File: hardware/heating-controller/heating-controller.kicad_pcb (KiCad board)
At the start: 2 copper layers, 81.8 x 85.9 mm, 22 parts, among them J1 LilyGo T-Display S3, J2 Temperature_probes, J3 Power connector, K1 FINDER-32.21-x000, Q1 AO3400A, U1 H11AA1

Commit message: First PCB, needs to be checked
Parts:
- added R1: 15k, Resistor_SMD:R_0603_1608Metric, F.Cu at (31.2, 17.8)
- added R5: 15k, Resistor_SMD:R_0603_1608Metric, F.Cu at (31.2, 22.5)
- C1: renamed from C2; footprint Resistor_SMD:R_0201_0603Metric -> Capacitor_SMD:C_0603_1608Metric
- moved R6 8.68 mm to (53.7, 45.6), turned to 0 degrees
- moved R4 0.85 mm to (31.8, 58.0)
- moved C1 0.23 mm to (43.4, 29.8)
- renumbered C3 to C2, C1 to C3, F2 to F1, F1 to F2, R3 to R2, R2 to R3, R1 to R4, R4 to R6, R5 to R7, R6 to R8, RV2 to RV1, RV1 to RV2
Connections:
- J2 pad 1: /EXT_TEMP_1 -> /EXT_TEMP
- J2 pad 3: /LIM_TEMP_1 -> /LIMITER_TEMP
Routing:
- net /LIMITER_TEMP: track 0.00 -> 111.6 mm, vias 0 -> 4
- net /EXT_TEMP: track 0.00 -> 102.1 mm, vias 0 -> 4
- net /RELAY_CMD: track 84.2 -> 96.4 mm
- net +3.3V: track 69.0 -> 58.2 mm
- net /HP_ACTIVE: track 74.3 -> 66.7 mm, vias 0 -> 2
- net +5V: track 96.5 -> 94.3 mm
- net /REL_NO: track 20.2 -> 18.2 mm
- net /REL_COM: track 36.4 -> 35.2 mm

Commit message: WIP
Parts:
- added D1: 1N4148WS, Diode_SMD:D_SOD-323, F.Cu at (74.8, 41.0)
- added D3: LED, LED_SMD:LED_0805_2012Metric, F.Cu at (95.2, 62.0)
- added J4: EXT_LED, Connector_PinHeader_2.54mm:PinHeader_1x02_P2.54mm_Vertical, F.Cu at (90.0, 63.6)
- added R7: 470, Resistor_SMD:R_0603_1608Metric, F.Cu at (85.8, 61.0)
- added R9: 470, Resistor_SMD:R_0603_1608Metric, F.Cu at (93.4, 59.1)
- C3: renamed from C2; footprint Capacitor_THT:C_Radial_D6.3mm_H7.0mm_P2.50mm -> Capacitor_THT:C_Radial_D10.0mm_H12.5mm_P5.00mm
- J1: renamed from J2; footprint Connector_Phoenix_MSTB:PhoenixContact_MSTBVA_2,5_4-G_1x04_P5.00mm_Vertical -> TerminalBlock_Phoenix:TerminalBlock_Phoenix_MKDS-3-4-5.08_1x04_P5.08mm_Horizontal
- J3: footprint Connector_Phoenix_MSTB:PhoenixContact_MSTBVA_2,5_7-G_1x07_P5.00mm_Vertical -> TerminalBlock_Phoenix:TerminalBlock_Phoenix_MKDS-3-7-5.08_1x07_P5.08mm_Horizontal
- R5: renamed from R2; footprint Resistor_THT:R_Axial_DIN0204_L3.6mm_D1.6mm_P5.08mm_Horizontal -> Resistor_THT:R_Axial_DIN0614_L14.3mm_D5.7mm_P15.24mm_Horizontal
- moved R5 41.8 mm to (29.1, 65.1), turned to 90 degrees
- moved RV2 35.6 mm to (24.1, 70.8)
- moved Q1 32.9 mm to (83.2, 88.2), turned to -90 degrees
- moved R8 32.4 mm to (78.2, 65.9)
- moved J2 31.7 mm to (46.8, 35.7)
- moved F2 31.6 mm to (25.3, 84.6)
- moved C3 30.3 mm to (68.0, 59.2)
- moved C2 29.2 mm to (64.5, 50.0)
- moved J3 28.9 mm to (25.7, 100.5)
- moved D2 28.7 mm to (64.6, 54.3)
- moved C1 28.5 mm to (75.1, 78.7)
- moved RV1 28.5 mm to (44.4, 79.7)
- moved PS1 28.5 mm to (36.0, 47.4)
- moved R2 28.5 mm to (48.9, 74.6)
- moved R3 28.5 mm to (52.0, 78.1)
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- renumbered C3 to C1, C1 to C2, D1 to D2, D2 to D4, F2 to F1, F1 to F2, J1 to J2, R8 to R10, R3 to R2, R4 to R3, R5 to R4, R7 to R8, RV2 to RV1, RV1 to RV2
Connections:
- J2 pad 12: +5V -> Net-(D1-Pad1)
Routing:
- net +3.3V: track 58.2 -> 10.0 mm
- net /RELAY_CMD: track 96.4 -> 49.6 mm
- net Net-(D3-Pad1): track 7.67 -> 50.2 mm
- net /EXT_TEMP: track 102.1 -> 123.8 mm, vias 4 -> 0
- net Net-(Q1-Pad1): track 6.73 -> 28.0 mm, vias 0 -> 2
- net /HP_ACTIVE: track 66.7 -> 77.0 mm
- net Net-(F2-Pad2): track 27.8 -> 18.8 mm
- net /REL_COM: track 35.2 -> 27.7 mm
- net +5V: track 94.3 -> 101.4 mm, vias 0 -> 2
- net /L: track 22.7 -> 16.1 mm
- net /LIMITER_TEMP: track 111.6 -> 118.1 mm, vias 4 -> 0
- net /N: track 54.3 -> 48.7 mm
- net Net-(F1-Pad2): track 19.5 -> 14.4 mm
- net Net-(D1-Pad1): track 0.00 -> 4.21 mm
- net Net-(J4-Pad2): track 0.00 -> 3.42 mm
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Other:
- outline, holes or cut-outs redrawn
- board text added: "https://github.com/BwanaFr/heating-controller"

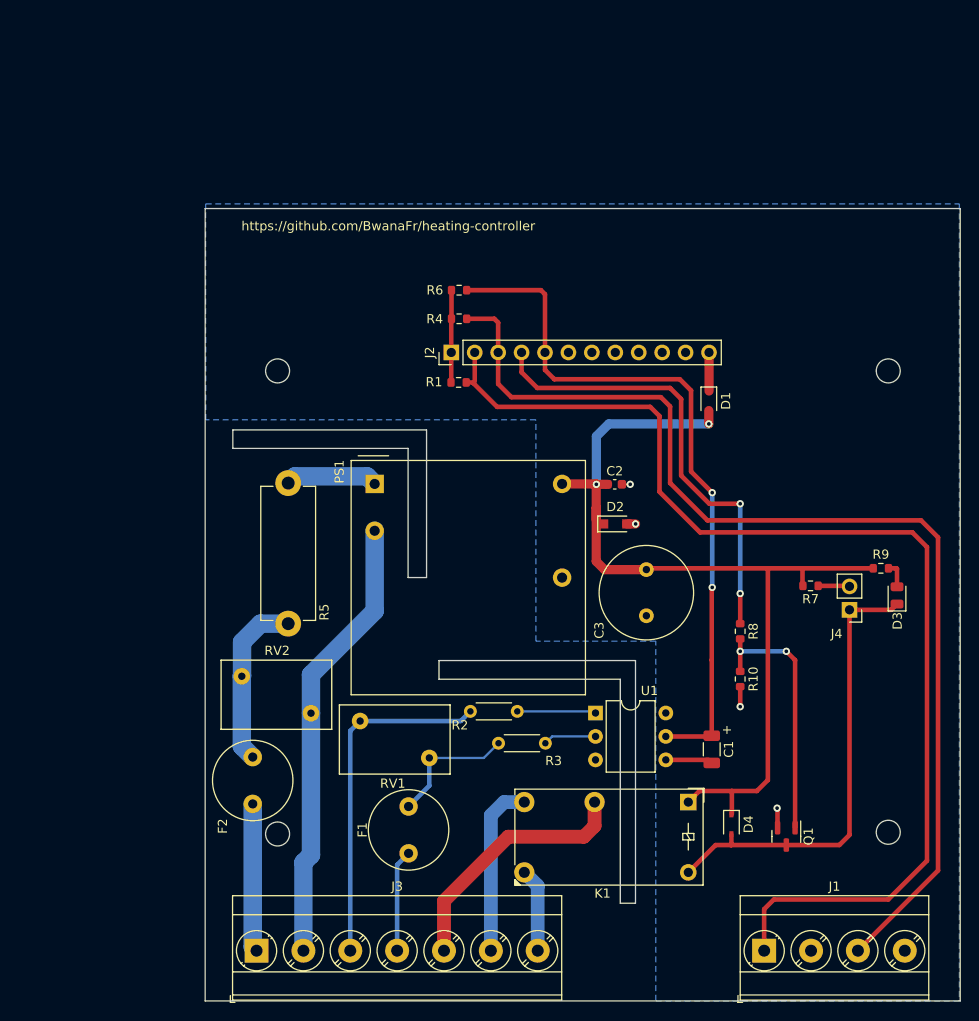
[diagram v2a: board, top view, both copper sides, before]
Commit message: Added 10uF capacitors to NTC
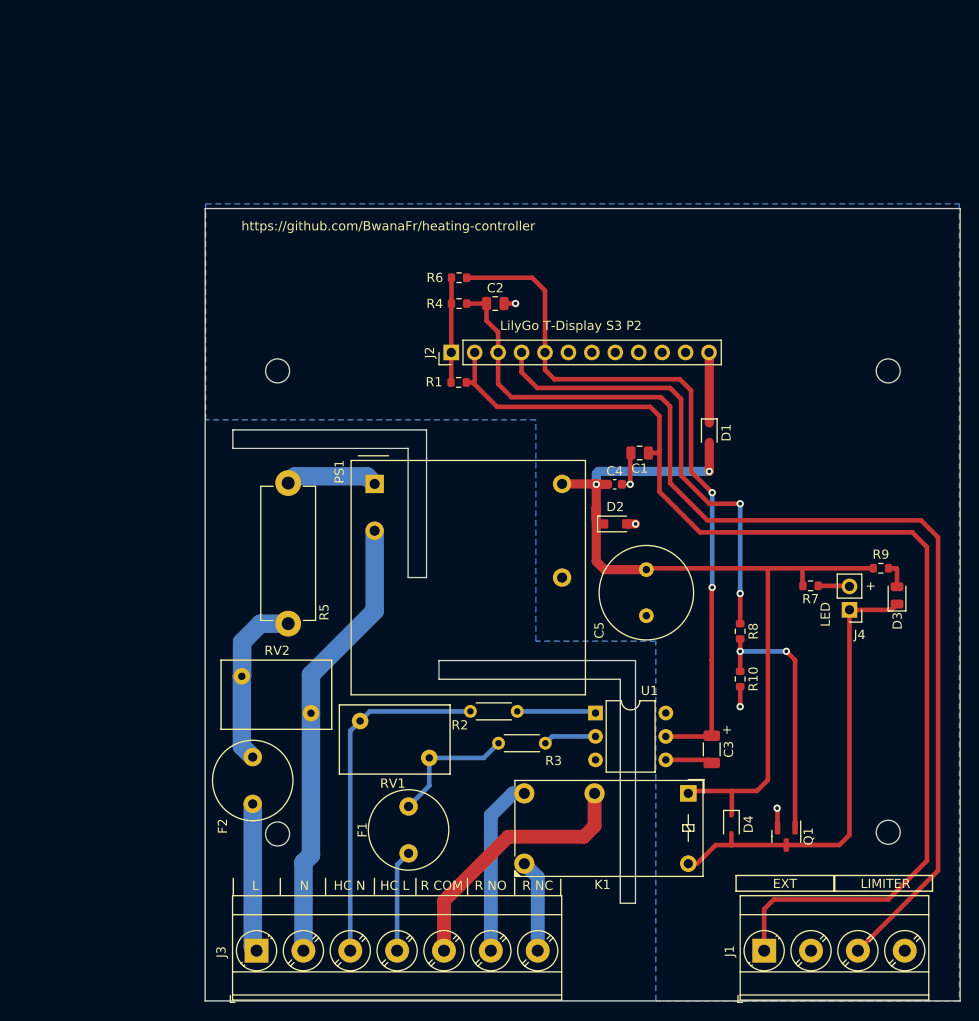
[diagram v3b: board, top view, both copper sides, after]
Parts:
- added C1: 10uF, Capacitor_SMD:C_0805_2012Metric, F.Cu at (67.2, 46.6)
- added C2: 10uF, Capacitor_SMD:C_0805_2012Metric, F.Cu at (51.6, 30.4)
- moved D1 3.45 mm to (74.8, 44.4)
- moved R4 1.65 mm to (47.7, 30.4)
- moved R6 1.35 mm to (47.7, 27.6)
- moved K1 0.94 mm to (72.5, 83.5)
- renumbered C1 to C3, C2 to C4, C3 to C5
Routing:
- net GND: track 11.3 -> 16.0 mm, vias 4 -> 5
- net Net-(D1-Pad1): track 4.21 -> 7.66 mm
- net +5V: track 101.4 -> 98.3 mm
- net +3.3V: track 10.0 -> 11.4 mm
- net /EXT_TEMP: track 123.8 -> 125.1 mm
- net /LIMITER_TEMP: track 118.1 -> 119.2 mm
- net /REL_NC: track 9.09 -> 10.0 mm
- net /REL_COM: track 27.7 -> 28.6 mm
- net /HP_ACTIVE: track 77.0 -> 77.8 mm
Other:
- board text added: "EXT"
- board text added: "HC L"
- board text added: "HC N"
- board text added: "L"
- board text added: "LED"
- board text added: "LIMITER"
- board text added: "LilyGo T-Display S3 P2"
- board text added: "N"
- board text added: "R COM"
- board text added: "R NC"
- board text added: "R NO"

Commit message: WIP
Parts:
- added J5: USER_LED, Connector_PinHeader_2.54mm:PinHeader_1x02_P2.54mm_Vertical, F.Cu at (87.8, 44.6)
- added Q1: AO3400A, Package_TO_SOT_SMD:SOT-23, F.Cu at (82.8, 44.6)
- added R11: 100k, Resistor_SMD:R_0603_1608Metric, F.Cu at (78.5, 44.7)
- added R13: 470, Resistor_SMD:R_0603_1608Metric, F.Cu at (82.1, 49.7)
- added R8: 1k, Resistor_SMD:R_0603_1608Metric, F.Cu at (81.8, 39.6)
- R10: renamed from R9; value 470 -> 2k
- renumbered D3 to D2, D2 to D3, Q1 to Q2, R10 to R12, R8 to R9
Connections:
- J1 pad 2: /EXT_TEMP_2 -> GND
- J1 pad 4: /LIM_TEMP_2 -> GND
- J2 pad 6: unconnected-(J2-Pad6) -> /USER_LED
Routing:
- net /USER_LED: track 0.00 -> 31.5 mm
- net Net-(J5-Pad2): track 0.00 -> 7.23 mm
- net +5V: track 98.3 -> 105.3 mm
- net Net-(Q1-Pad1): track 0.00 -> 6.71 mm
- net Net-(J5-Pad1): track 0.00 -> 4.12 mm
- net GND: track 16.0 -> 19.4 mm, vias 5 -> 6
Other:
- board text added: "REL_LED"
- board text added: "USER_LED"
- board text removed: "LED"

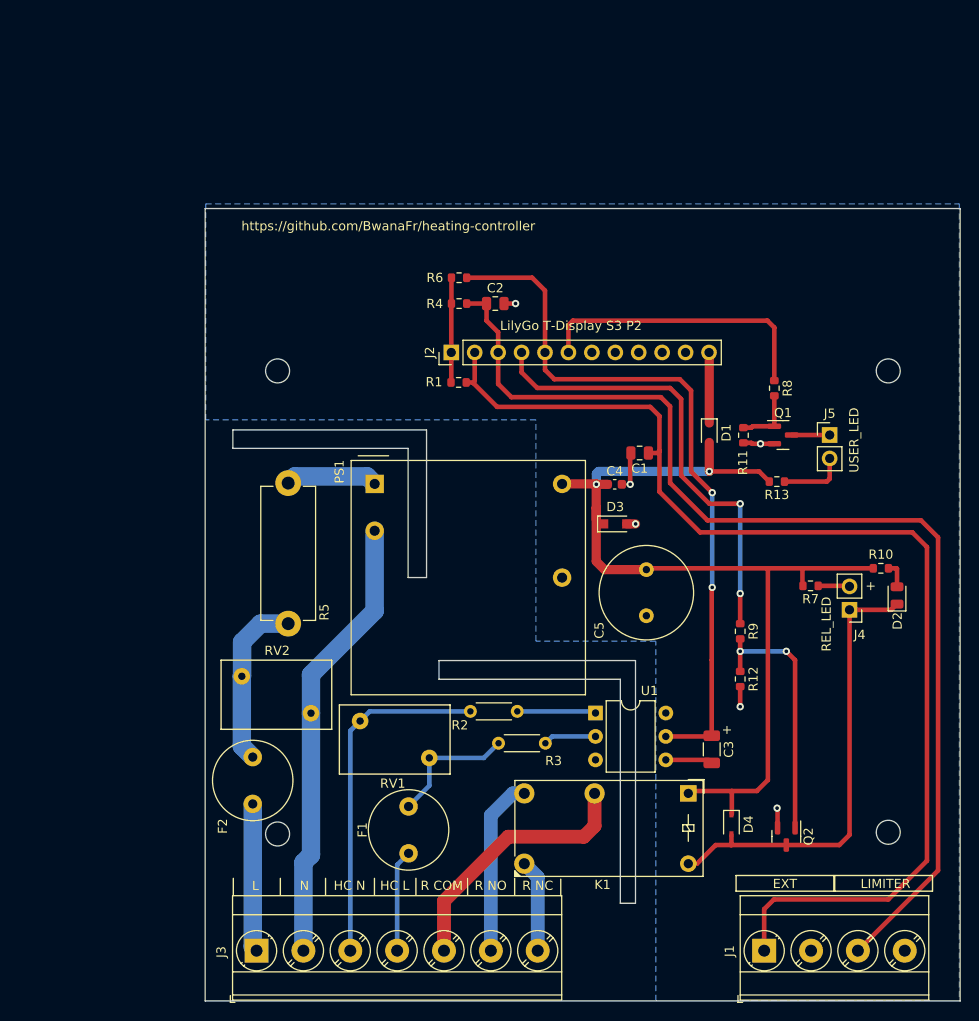
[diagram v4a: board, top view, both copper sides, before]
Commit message: Migrated to KiCad 7 and remove custom AC/DC
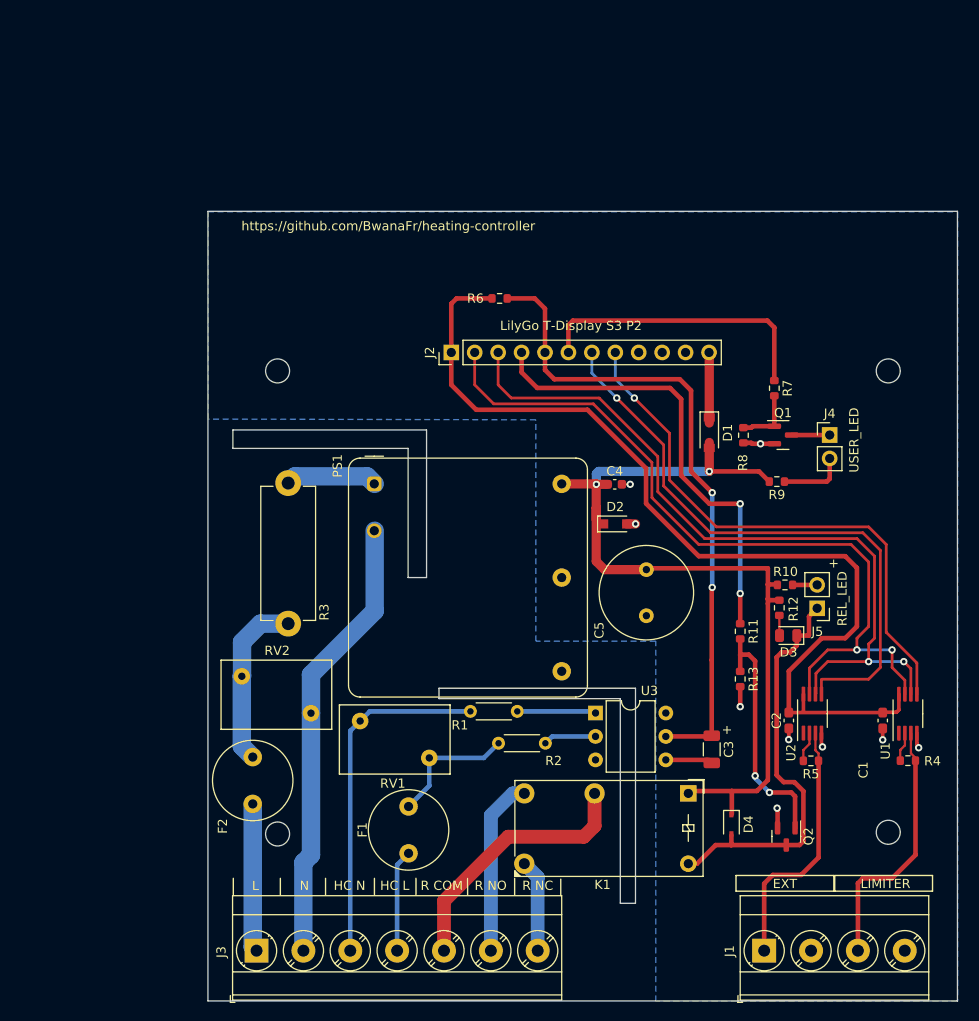
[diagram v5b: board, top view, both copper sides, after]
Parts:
- removed the R4 at (47.7, 30.4)
- added R5: 15k, Resistor_SMD:R_0603_1608Metric, F.Cu at (85.8, 80.0)
- added U1: MAX6682, Package_SO:MSOP-8_3x3mm_P0.65mm, F.Cu at (96.3, 74.9)
- added U2: MAX6682, Package_SO:MSOP-8_3x3mm_P0.65mm, F.Cu at (86.0, 74.8)
- C1, C2: value 10uF -> 100nF; footprint Capacitor_SMD:C_0805_2012Metric -> Capacitor_SMD:C_0603_1608Metric_Pad1.08x0.95mm_HandSolder
- D1: value 1N4148WS -> Schottky; footprint Diode_SMD:D_SOD-323 -> Diode_SMD:D_SOD-123
- PS1: footprint heating-controller:Converter_ACDC_aimtec_AMEM5 -> Converter_ACDC:Converter_ACDC_Murata_BAC05SxxDC_THT
- moved R4 63.7 mm to (96.3, 80.0), turned to 180 degrees
- moved C2 55.3 mm to (83.4, 75.6), turned to -90 degrees
- moved C1 39.2 mm to (93.6, 75.6), turned to -90 degrees
- moved D3 12.6 mm to (83.3, 66.4), turned to 180 degrees
- moved R12 11.8 mm to (82.4, 63.4), turned to 90 degrees
- moved R6 4.94 mm to (52.1, 29.8)
- moved PS1 3.57 mm to (38.5, 49.9)
- moved J5 3.51 mm to (86.5, 63.4)
- moved R10 2.77 mm to (83.0, 60.9)
- renumbered D3 to D2, D2 to D3, J5 to J4, J4 to J5, R2 to R1, R7 to R10, R9 to R11, R10 to R12, R12 to R13, R3 to R2, R5 to R3, R1 to R4, R8 to R7, R11 to R8, R13 to R9, U1 to U3
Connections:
- C1 pad 1: /EXT_TEMP -> +3.3V
- C2 pad 1: /LIMITER_TEMP -> +3.3V
- J1 pad 3: /LIMITER_TEMP -> /LIM_TEMP
- J2 pad 2: /EXT_TEMP -> /SCK
- J2 pad 3: /LIMITER_TEMP -> /SO
- J2 pad 7: unconnected-(J2-Pad7) -> /~{EXT_CS}
- J2 pad 8: unconnected-(J2-Pad8) -> /~{LIM_CS}
- R4 pad 1: +3.3V -> /LIM_TEMP
- R4 pad 2: /EXT_TEMP -> Net-(R4-Pad2)
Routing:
- net /LIMITER_TEMP: track 119.2 -> 0.00 mm
- net /EXT_TEMP: track 125.1 -> 28.0 mm
- net +3.3V: track 11.4 -> 103.8 mm
- net /SCK: track 0.00 -> 84.4 mm, vias 0 -> 2
- net /SO: track 0.00 -> 82.1 mm, vias 0 -> 2
- net /~{EXT_CS}: track 0.00 -> 65.2 mm, vias 0 -> 1
- net /~{LIM_CS}: track 0.00 -> 60.3 mm, vias 0 -> 1
- net /LIM_TEMP: track 0.00 -> 28.2 mm
- net +5V: track 105.3 -> 94.3 mm
- net /HP_ACTIVE: track 77.8 -> 71.4 mm
- net Net-(D3-Pad1): track 49.8 -> 44.9 mm
- net Net-(R5-Pad2): track 0.00 -> 3.28 mm
- net Net-(R4-Pad2): track 0.00 -> 3.18 mm
- net Net-(Q2-Pad1): track 28.0 -> 26.7 mm
- net GND: track 19.4 -> 20.6 mm, vias 6 -> 9
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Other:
- board size 81.8 x 85.9 mm -> 81.2 x 85.6 mm

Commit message: MAX682 hardware
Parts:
- added R14: 10k, Resistor_SMD:R_0603_1608Metric, F.Cu at (99.3, 74.3)
- added R15: 10k, Resistor_SMD:R_0603_1608Metric, F.Cu at (90.1, 73.5)
- R4, R5: value 15k -> 1.2k
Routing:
- net +3.3V: track 103.8 -> 109.7 mm
- net /~{EXT_CS}: track 65.2 -> 67.8 mm
- net /~{LIM_CS}: track 60.3 -> 62.6 mm
- net Net-(D3-K): track 44.9 -> 46.9 mm
- net +5V: track 94.3 -> 93.7 mm
- net Net-(D1-K): track 7.66 -> 7.10 mm
